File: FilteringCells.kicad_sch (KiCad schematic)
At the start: 0 parts

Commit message: feat: add filtering components in library
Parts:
- added J?: S7B-XH-A, CONN_S7B-XH-A_JST, symbol FixedWing:S7B-XH-A
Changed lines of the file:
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@@
 (kicad_sch (version 20230121) (generator eeschema)
   (paper "A4")
+  (symbol (lib_id "FixedWing:S7B-XH-A") (at 43.18 83.82 0) (mirror y) (unit 1)
+    (in_bom yes) (on_board yes) (dnp no)
+    (property "Reference" "J?" (at 35.56 78.74 0)
+      (effects (font (size 1.524 1.524)) (justify left))
+    )
+    (property "Value" "S7B-XH-A" (at 39.37 104.14 0)
+      (effects (font (size 1.524 1.524)) (justify left))
+    )
+    (property "Footprint" "CONN_S7B-XH-A_JST" (at 46.99 77.47 0)
+      (effects (font (size 1.27 1.27) italic) hide)
+    )
+    (property "Datasheet" "S7B-XH-A" (at 46.99 80.01 0)
+      (effects (font (size 1.27 1.27) italic) hide)
+    )
+    (pin "3")
+    (pin "4")
+    (pin "2")
+    (pin "5")
+    (pin "1")
+    (pin "7")
+    (pin "6")
+    (instances
+      (project "bms-board"
+        (path "/8a7831d1-a913-4f04-8780-225d2234b41d/95f820cc-7b9f-45ce-aa8e-ca8cb50aec5e"
+          (reference "J?") (unit 1)
+        )
+      )
+    )
+  )
 )

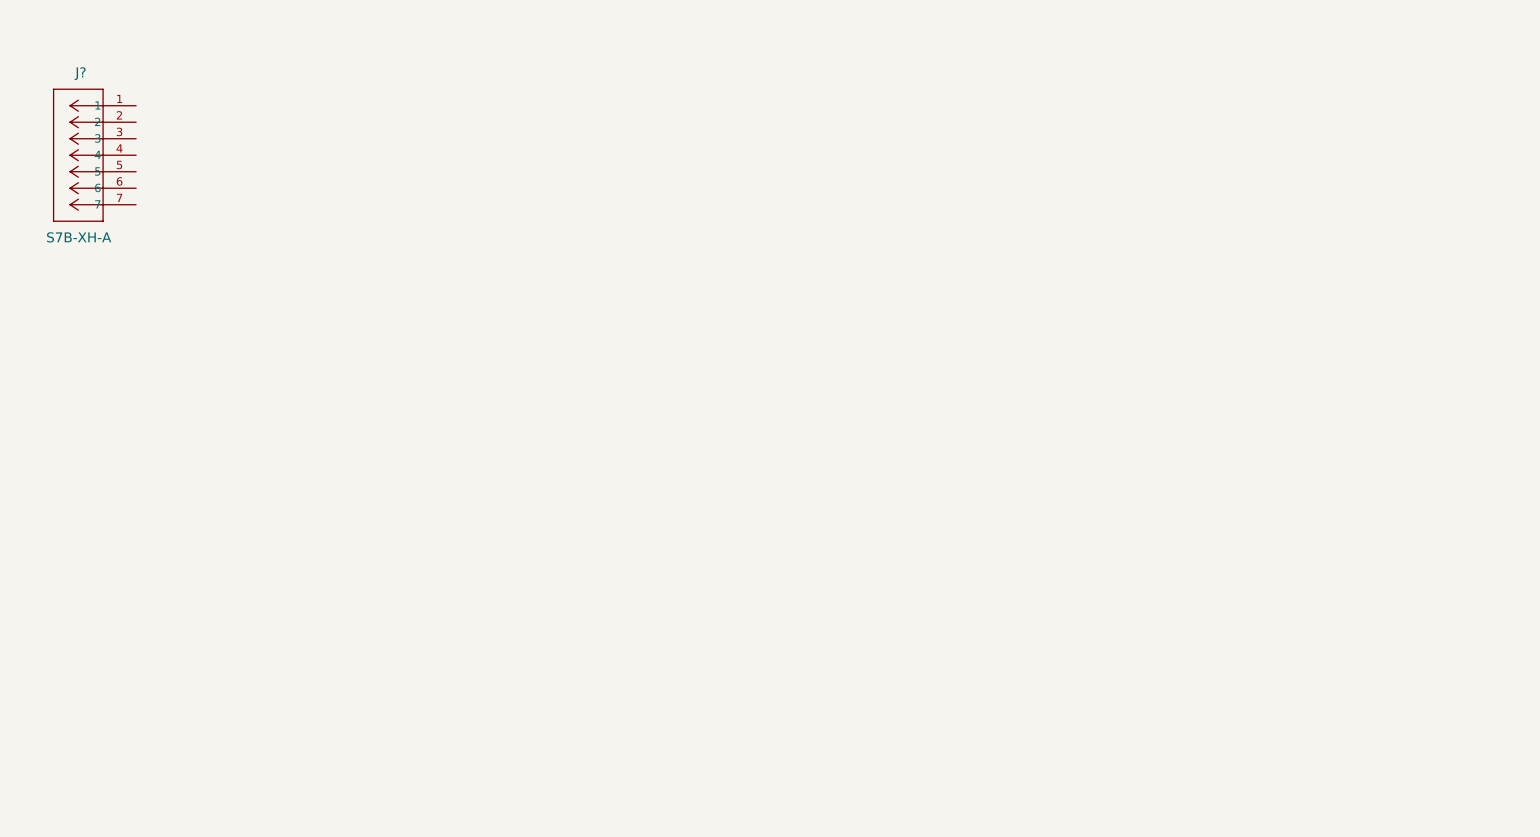
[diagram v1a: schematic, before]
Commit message: feat: add more symbols, some traces, sheet template
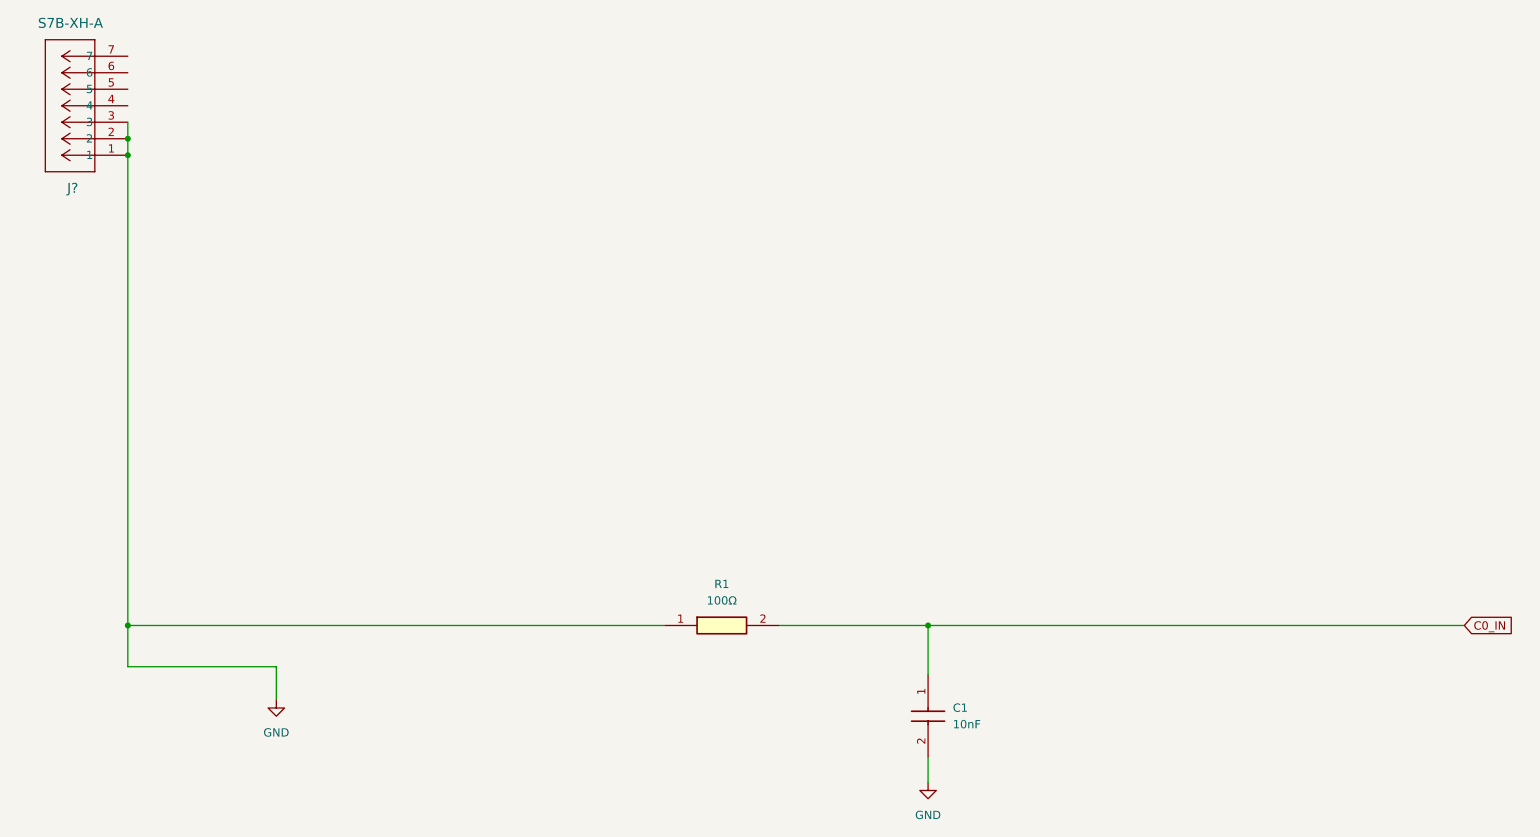
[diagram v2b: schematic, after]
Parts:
- added C1: 10nF, CAPC2012X95N, symbol FixedWing:AC0805KRX7R8BB103
- added R1: 100Ω, RESC2012X50N, symbol FixedWing:CRCW0805100RFKEA
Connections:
- net GND: now reaches J?.1
- net GND: now also J?.2, J?.3, C1.2, R1.1
- new net C0_IN: C1.1, R1.2
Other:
- moved on the sheet: J?
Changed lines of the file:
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@@
 (kicad_sch (version 20230121) (generator eeschema)
   (paper "A4")
-  (symbol (lib_id "FixedWing:S7B-XH-A") (at 43.18 83.82 0) (mirror y) (unit 1)
+  (junction (at 165.1 163.83) (diameter 0) (color 0 0 0 0)
+  )
+  (junction (at 41.91 91.44) (diameter 0) (color 0 0 0 0)
+  )
+  (junction (at 41.91 163.83) (diameter 0) (color 0 0 0 0)
+  )
+  (junction (at 41.91 88.9) (diameter 0) (color 0 0 0 0)
+  )
+  (wire (pts (xy 64.77 170.18) (xy 64.77 175.26))
+    (stroke (width 0) (type default))
+  )
+  (wire (pts (xy 41.91 86.36) (xy 41.91 88.9))
+    (stroke (width 0) (type default))
+  )
+  (wire (pts (xy 41.91 170.18) (xy 64.77 170.18))
+    (stroke (width 0) (type default))
+  )
+  (wire (pts (xy 41.91 163.83) (xy 41.91 170.18))
+    (stroke (width 0) (type default))
+  )
+  (wire (pts (xy 41.91 91.44) (xy 41.91 163.83))
+    (stroke (width 0) (type default))
+  )
+  (wire (pts (xy 165.1 184.15) (xy 165.1 187.96))
+    (stroke (width 0) (type default))
+  )
+  (wire (pts (xy 41.91 88.9) (xy 41.91 91.44))
+    (stroke (width 0) (type default))
+  )
+  (wire (pts (xy 142.24 163.83) (xy 165.1 163.83))
+    (stroke (width 0) (type default))
+  )
+  (wire (pts (xy 165.1 163.83) (xy 247.65 163.83))
+    (stroke (width 0) (type default))
+  )
+  (wire (pts (xy 165.1 163.83) (xy 165.1 171.45))
+    (stroke (width 0) (type default))
+  )
+  (wire (pts (xy 41.91 163.83) (xy 124.46 163.83))
+    (stroke (width 0) (type default))
+  )
+  (global_label "C0_IN" (shape input) (at 247.65 163.83 0) (fields_autoplaced)
+    (effects (font (size 1.27 1.27)) (justify left))
+    (property "Intersheetrefs" "${INTERSHEET_REFS}" (at 256.0176 163.83 0)
+      (effects (font (size 1.27 1.27)) (justify left) hide)
+    )
+  )
+  (symbol (lib_id "power:GND") (at 64.77 175.26 0) (unit 1)
+    (in_bom yes) (on_board yes) (dnp no) (fields_autoplaced)
+    (property "Reference" "#PWR02" (at 64.77 181.61 0)
+      (effects (font (size 1.27 1.27)) hide)
+    )
+    (property "Value" "GND" (at 64.77 180.34 0)
+      (effects (font (size 1.27 1.27)))
+    )
+    (property "Footprint" "" (at 64.77 175.26 0)
+      (effects (font (size 1.27 1.27)) hide)
+    )
+    (property "Datasheet" "" (at 64.77 175.26 0)
+      (effects (font (size 1.27 1.27)) hide)
+    )
+    (pin "1")
+    (instances
+      (project "bms-board"
+        (path "/8a7831d1-a913-4f04-8780-225d2234b41d/95f820cc-7b9f-45ce-aa8e-ca8cb50aec5e"
+          (reference "#PWR02") (unit 1)
+        )
+      )
+    )
+  )
+  (symbol (lib_id "FixedWing:AC0805KRX7R8BB103") (at 165.1 171.45 270) (unit 1)
+    (in_bom yes) (on_board yes) (dnp no) (fields_autoplaced)
+    (property "Reference" "C1" (at 168.91 176.53 90)
+      (effects (font (size 1.27 1.27)) (justify left))
+    )
+    (property "Value" "10nF" (at 168.91 179.07 90)
+      (effects (font (size 1.27 1.27)) (justify left))
+    )
+    (property "Footprint" "CAPC2012X95N" (at 68.91 180.34 0)
+      (effects (font (size 1.27 1.27)) (justify left top) hide)
+    )
+    (property "Datasheet" "https://www.yageo.com/en/ProductSearch/PartNumberSearch?part_number=AC0805KRX7R8BB103" (at -31.09 180.34 0)
+      (effects (font (size 1.27 1.27)) (justify left top) hide)
+    )
+    (property "Height" "0.95" (at -231.09 180.34 0)
+      (effects (font (size 1.27 1.27)) (justify left top) hide)
+    )
+    (property "Mouser Part Number" "603-AC805KRX7R8BB103" (at -331.09 180.34 0)
+      (effects (font (size 1.27 1.27)) (justify left top) hide)
+    )
+    (property "Mouser Price/Stock" "https://www.mouser.co.uk/ProductDetail/YAGEO/AC0805KRX7R8BB103?qs=WS5Jv%252B%252Bx1qWanT8XqjMqIQ%3D%3D" (at -431.09 180.34 0)
+      (effects (font (size 1.27 1.27)) (justify left top) hide)
+    )
+    (property "Manufacturer_Name" "YAGEO" (at -531.09 180.34 0)
+      (effects (font (size 1.27 1.27)) (justify left top) hide)
+    )
+    (property "Manufacturer_Part_Number" "AC0805KRX7R8BB103" (at -631.09 180.34 0)
+      (effects (font (size 1.27 1.27)) (justify left top) hide)
+    )
+    (pin "2")
+    (pin "1")
+    (instances
+      (project "bms-board"
+        (path "/8a7831d1-a913-4f04-8780-225d2234b41d/95f820cc-7b9f-45ce-aa8e-ca8cb50aec5e"
+          (reference "C1") (unit 1)
+        )
+      )
+    )
+  )
+  (symbol (lib_id "FixedWing:S7B-XH-A") (at 41.91 91.44 180) (unit 1)
     (in_bom yes) (on_board yes) (dnp no)
-    (property "Reference" "J?" (at 35.56 78.74 0)
+    (property "Reference" "J?" (at 34.29 96.52 0)
       (effects (font (size 1.524 1.524)) (justify left))
     )
-    (property "Value" "S7B-XH-A" (at 39.37 104.14 0)
+    (property "Value" "S7B-XH-A" (at 38.1 71.12 0)
       (effects (font (size 1.524 1.524)) (justify left))
     )
-    (property "Footprint" "CONN_S7B-XH-A_JST" (at 46.99 77.47 0)
+    (property "Footprint" "CONN_S7B-XH-A_JST" (at 45.72 97.79 0)
       (effects (font (size 1.27 1.27) italic) hide)
     )
-    (property "Datasheet" "S7B-XH-A" (at 46.99 80.01 0)
+    (property "Datasheet" "S7B-XH-A" (at 45.72 95.25 0)
       (effects (font (size 1.27 1.27) italic) hide)
     )
@@
         )
       )
+    )
+  )
+  (symbol (lib_id "power:GND") (at 165.1 187.96 0) (unit 1)
+    (in_bom yes) (on_board yes) (dnp no) (fields_autoplaced)
+    (property "Reference" "#PWR03" (at 165.1 194.31 0)
+      (effects (font (size 1.27 1.27)) hide)
+    )
+    (property "Value" "GND" (at 165.1 193.04 0)
+      (effects (font (size 1.27 1.27)))
+    )
+    (property "Footprint" "" (at 165.1 187.96 0)
+      (effects (font (size 1.27 1.27)) hide)
+    )
+    (property "Datasheet" "" (at 165.1 187.96 0)
+      (effects (font (size 1.27 1.27)) hide)
+    )
+    (pin "1")
+    (instances
+      (project "bms-board"
+        (path "/8a7831d1-a913-4f04-8780-225d2234b41d/95f820cc-7b9f-45ce-aa8e-ca8cb50aec5e"
+          (reference "#PWR03") (unit 1)
+        )
+      )
+    )
+  )
+  (symbol (lib_id "FixedWing:CRCW0805100RFKEA") (at 124.46 163.83 0) (unit 1)
+    (in_bom yes) (on_board yes) (dnp no) (fields_autoplaced)
+    (property "Reference" "R1" (at 133.35 157.48 0)
+      (effects (font (size 1.27 1.27)))
+    )
+    (property "Value" "100Ω" (at 133.35 160.02 0)
+      (effects (font (size 1.27 1.27)))
+    )
+    (property "Footprint" "RESC2012X50N" (at 138.43 260.02 0)
+      (effects (font (size 1.27 1.27)) (justify left top) hide)
+    )
+    (property "Datasheet" "http://www.vishay.com/docs/20035/dcrcwe3.pdf" (at 138.43 360.02 0)
+      (effects (font (size 1.27 1.27)) (justify left top) hide)
+    )
+    (property "Height" "0.5" (at 138.43 560.02 0)
+      (effects (font (size 1.27 1.27)) (justify left top) hide)
+    )
+    (property "Mouser Part Number" "71-CRCW0805-100-E3" (at 138.43 660.02 0)
+      (effects (font (size 1.27 1.27)) (justify left top) hide)
+    )
+    (property "Mouser Price/Stock" "https://www.mouser.co.uk/ProductDetail/Vishay-Dale/CRCW0805100RFKEA?qs=LOX6nxTstiYDPDKmuLyNLw%3D%3D" (at 138.43 760.02 0)
+      (effects (font (size 1.27 1.27)) (justify left top) hide)
+    )
+    (property "Manufacturer_Name" "Vishay" (at 138.43 860.02 0)
+      (effects (font (size 1.27 1.27)) (justify left top) hide)
+    )
+    (property "Manufacturer_Part_Number" "CRCW0805100RFKEA" (at 138.43 960.02 0)
+      (effects (font (size 1.27 1.27)) (justify left top) hide)
+    )
+    (pin "2")
+    (pin "1")
+    (instances
+      (project "bms-board"
+        (path "/8a7831d1-a913-4f04-8780-225d2234b41d/95f820cc-7b9f-45ce-aa8e-ca8cb50aec5e"
+          (reference "R1") (unit 1)
+        )
+      )
